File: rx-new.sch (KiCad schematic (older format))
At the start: 124 parts, among them J1 RF_IN, J2 PWR, J3 IQ_OUT, J4 4LO_IN, J5 RX_GAIN, Q1 BC848, Q2 BC858, Q3 BC848, Q4 BC858, Q5 2N7002, Q6 2N7002, U1 TPS79101DBVREP, U2 SN74CBT3253, U3 AD797, U4 AD797, U5 NC7SZ00M5X, U6 OPA1662, U7 74AUP1G74, U8 74AUP1G74, U9 4052

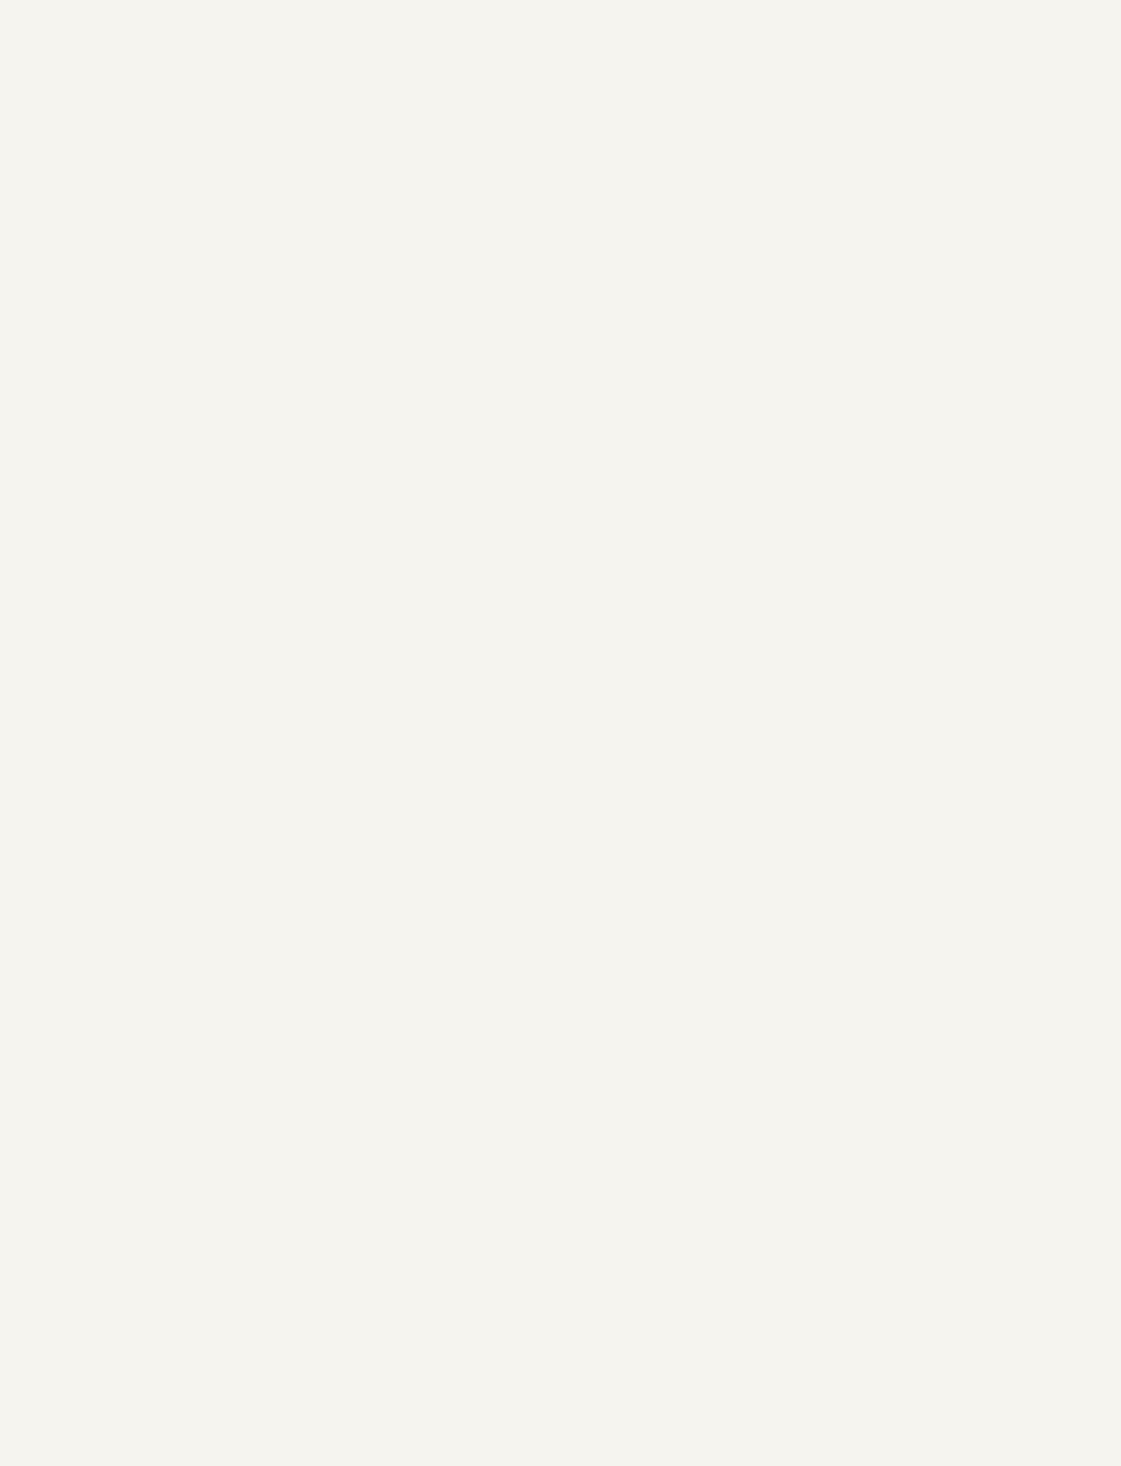
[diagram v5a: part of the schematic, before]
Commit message: WIP: added TX exciter draft
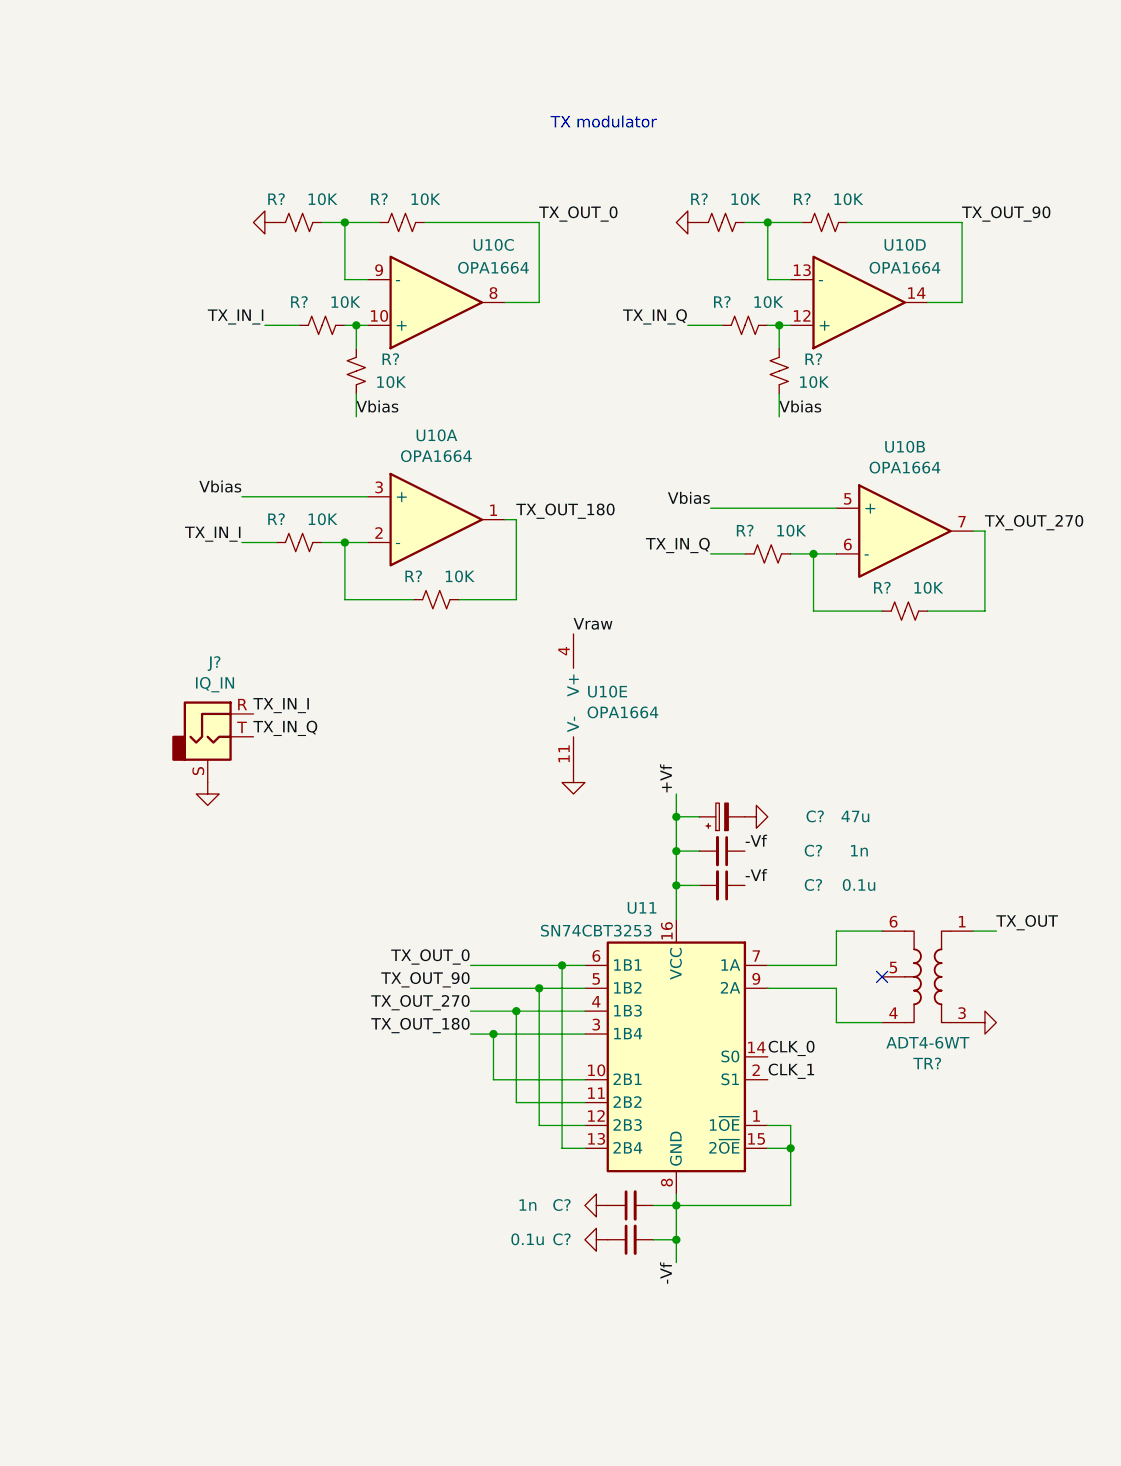
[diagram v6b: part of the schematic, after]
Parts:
- added C? (x2): 0.1u, Capacitor_SMD:C_0805_2012Metric_Pad1.15x1.40mm_HandSolder, symbol Device:C_Small
- added C? (x2): 1n, Capacitor_SMD:C_0805_2012Metric_Pad1.15x1.40mm_HandSolder, symbol Device:C_Small
- added C?: 47u, custom_library:CP_1210_3225Metric_Pad1.42x2.65mm_HandSolder, symbol Device:CP_Small
- added J?: IQ_IN, Connector_Audio:Jack_3.5mm_CUI_SJ1-3533NG_Horizontal, symbol custom_library:SJ1-3533NG
- added R? (x12): 10K, Resistor_SMD:R_0805_2012Metric_Pad1.15x1.40mm_HandSolder, symbol Device:R_Small_US
- added TR?: ADT4-6WT, RF_Mini-Circuits:Mini-Circuits_CD636_H4.11mm, symbol Transformer:ADT4-6WT
- added U10: OPA1664, symbol Device:Opamp_Quad_Generic
- added U11: SN74CBT3253, Package_SO:SOP-16_4.4x10.4mm_P1.27mm, symbol Analog_Switch:SN74CBT3253
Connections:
- net +Vf: now also C?.1, C?.2, C?.2, U11.16 (VCC)
- net -Vf: now also C?.1, C?.1, C?.2, C?.2, U11.1 (1~OE), U11.15 (2~OE), U11.8 (GND)
- net CLK_0: now also U11.14 (S0)
- net CLK_1: now also U11.2 (S1)
- net GND: now also C?.1, C?.1, C?.2, J?.S, R?.1, R?.1, TR?.3, U10.11 (V-)
- net Vbias: now also R?.2, R?.2, U10.3 (+), U10.5 (+)
- net Vraw: now also U10.4 (V+)
- new net: TR?.6, U11.7 (1A)
- new net: TR?.4, U11.9 (2A)
- new net: R?.1, R?.2, U10.2 (-)
- new net: R?.1, R?.2, U10.6 (-)
- new net: R?.1, R?.2, U10.10 (+)
- new net: R?.2, R?.2, U10.9 (-)
- new net: R?.1, R?.2, U10.12 (+)
- new net: R?.2, R?.2, U10.13 (-)
- new net TX_IN_I: J?.R, R?.1, R?.2
- new net TX_IN_Q: J?.T, R?.1, R?.2
- new net TX_OUT: TR?.1
- new net TX_OUT_0: R?.1, U10.8, U11.13 (2B4), U11.6 (1B1)
- new net TX_OUT_180: R?.1, U10.1, U11.10 (2B1), U11.3 (1B4)
- new net TX_OUT_270: R?.1, U10.7, U11.11 (2B2), U11.4 (1B3)
- new net TX_OUT_90: R?.1, U10.14, U11.12 (2B3), U11.5 (1B2)
- no-connect marks 6 -> 7
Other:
- note added: "TX modulator"

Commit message: changed_a_lot
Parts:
- removed C13: 0.01u, Capacitor_SMD:C_0805_2012Metric_Pad1.15x1.40mm_HandSolder, symbol Device:C_Small
- removed C20, C49, C?: 47u, custom_library:CP_1210_3225Metric_Pad1.42x2.65mm_HandSolder, symbol Device:CP_Small
- removed C42: 1n, Capacitor_SMD:C_0805_2012Metric_Pad1.15x1.40mm_HandSolder, symbol Device:C_Small
- removed D2: 1N4148, symbol Device:D_Small_ALT
- removed Q3: BC848, Package_TO_SOT_SMD:SOT-23, symbol Transistor_BJT:BC848
- removed R25: 100k, Resistor_SMD:R_0805_2012Metric_Pad1.15x1.40mm_HandSolder, symbol Device:R_Small_US
- removed R26, R? (x9): 10K, Resistor_SMD:R_0805_2012Metric_Pad1.15x1.40mm_HandSolder, symbol Device:R_Small_US
- removed R29: 330K, Resistor_SMD:R_0805_2012Metric_Pad1.15x1.40mm_HandSolder, symbol Device:R_Small_US
- removed R3: 1.6k, Resistor_SMD:R_0805_2012Metric_Pad1.15x1.40mm_HandSolder, symbol Device:R_Small_US
- removed R30: 180K, Resistor_SMD:R_0805_2012Metric_Pad1.15x1.40mm_HandSolder, symbol Device:R_Small_US
- removed R4: 750, Resistor_SMD:R_0805_2012Metric_Pad1.15x1.40mm_HandSolder, symbol Device:R_Small_US
- removed R8: 120k, Resistor_SMD:R_0805_2012Metric_Pad1.15x1.40mm_HandSolder, symbol Device:R_Small_US
- removed R9: 33K, Resistor_SMD:R_0805_2012Metric_Pad1.15x1.40mm_HandSolder, symbol Device:R_Small_US
- removed U1: TPS79101DBVREP, custom_library:Texas_Instruments-TPS79101DBVREP-Level_A, symbol custom_library:TPS79101DBVREP
- removed unit 2 of U10
- removed unit 3 of U10
- removed unit 4 of U10
- added C? (x6): 1n, Capacitor_SMD:C_0805_2012Metric_Pad1.15x1.40mm_HandSolder, symbol Device:C_Small
- added C? (x3): 0.1u, Capacitor_SMD:C_0805_2012Metric_Pad1.15x1.40mm_HandSolder, symbol Device:C_Small
- added C?: 47u, custom_library:CP_1210_3225Metric_Pad1.42x2.65mm_HandSolder, symbol Device:CP_Small
- added C?: NF, custom_library:CP_1210_3225Metric_Pad1.42x2.65mm_HandSolder, symbol Device:CP_Small
- added Q? (x3): BC848, Package_TO_SOT_SMD:SOT-23, symbol Transistor_BJT:BC848
- added Q?: BC327, Package_TO_SOT_THT:TO-92_Inline, symbol Transistor_BJT:BC327
- added Q? (x2): BC858, Package_TO_SOT_SMD:SOT-23, symbol Transistor_BJT:BC858
- added Q? (x4): 2N7002, Package_TO_SOT_SMD:SOT-23, symbol Transistor_FET:2N7002
- added R? (x9): 10K, Resistor_SMD:R_0805_2012Metric_Pad1.15x1.40mm_HandSolder, symbol Device:R_Small_US
- added R? (x4): 47, Resistor_SMD:R_0805_2012Metric_Pad1.15x1.40mm_HandSolder, symbol Device:R_Small_US
- added R?: 18k?, Resistor_SMD:R_0805_2012Metric_Pad1.15x1.40mm_HandSolder, symbol Device:R_Small_US
- added R? (x2): 10k, Resistor_SMD:R_0805_2012Metric_Pad1.15x1.40mm_HandSolder, symbol Device:R_Small_US
- added R?: 27k, Resistor_SMD:R_0805_2012Metric_Pad1.15x1.40mm_HandSolder, symbol Device:R_Small_US
- added R?: 1.8k, Resistor_SMD:R_0805_2012Metric_Pad1.15x1.40mm_HandSolder, symbol Device:R_Small_US
- added R? (x5): 1M, Resistor_SMD:R_0805_2012Metric_Pad1.15x1.40mm_HandSolder, symbol Device:R_Small_US
- added R?: 100k, Resistor_SMD:R_0805_2012Metric_Pad1.15x1.40mm_HandSolder, symbol Device:R_Small_US
- added R? (x3): 330k, Resistor_SMD:R_0805_2012Metric_Pad1.15x1.40mm_HandSolder, symbol Device:R_Small_US
- added R?: 1E, Resistor_SMD:R_0805_2012Metric_Pad1.15x1.40mm_HandSolder, symbol Device:R_Small_US
- added R? (x2): 820k, Resistor_SMD:R_0805_2012Metric_Pad1.15x1.40mm_HandSolder, symbol Device:R_Small_US
- added R?: 47k, Resistor_SMD:R_0805_2012Metric_Pad1.15x1.40mm_HandSolder, symbol Device:R_Small_US
- added R? (x3): NF, Resistor_SMD:R_0805_2012Metric_Pad1.15x1.40mm_HandSolder, symbol Device:R_Small_US
- added R?: 27E, Resistor_SMD:R_0805_2012Metric_Pad1.15x1.40mm_HandSolder, symbol Device:R_Small_US
- added R? (x2): 33k, Resistor_SMD:R_0805_2012Metric_Pad1.15x1.40mm_HandSolder, symbol Device:R_Small_US
- added U? (x3): OPA1664, symbol Device:Opamp_Quad_Generic
- added U?: LM4040DBZ-3, Package_TO_SOT_SMD:SOT-23, symbol Reference_Voltage:LM4040DBZ-3
- C30: value 47u -> NF
- R10: value 10k -> 33k
- R11: value 10k -> 33kk
- R27: value 10k -> 100k
- R28: value 47k -> 330k
- R6: value 10k -> NF
- R7: value 22E -> 1E
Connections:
- net +9V: no longer C50.2, C51.2, R12.2, R13.2, U9.16 (VDD)
- net +Vd: now also R5.2; no longer R5.1
- net +Vf: now also C50.2, C51.2, R12.2, R13.2, R?.2, U9.16 (VDD), C?.2, Q?.1 (C), Q?.2 (E), R?.1, R?.1, R?.1, R?.1, R?.2, R?.2, R?.2, R?.2
- net -Vf: now also R?.2; no longer U11.1 (1~OE), U11.15 (2~OE), U2.1 (1~OE), U2.15 (2~OE)
- net 270deg: no longer R39.2, R40.2, R41.2, R42.2
- net 90deg: now also R39.2, R40.2, R41.2, R42.2
- net Eo: now also Q?.3 (D), Q?.3 (D), R?.1
- net GND: now also C?.1, C?.1, C?.1, C?.1, C?.1, C?.1, C?.1, C?.1, C?.2, C?.2, Q?.2 (E), Q?.2 (S), Q?.2 (S), Q?.2 (S), Q?.2 (S), R?.1, R?.1, R?.1, R?.1, R?.1, R?.2, R?.2, R?.2, R?.2, U?.2 (A)
- net Vbat: now also Q4.2 (E), R27.2, Q?.2 (E), Q?.3 (C), Q?.3 (E), R?.1
- net at C30.1, C31.2, C32.2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: no longer C34.2, C35.2, U4.7 (V+)
- net at C4.1, Q2.1 (B): now also R?.2
- net at C1.1, Q1.2 (E): now also R5.1; no longer R5.2
- net at R13.1, U9.9 (B): now also R34.1; no longer R34.2
- net at Q6.3 (D): now also R34.2; no longer R34.1
- net at R?.1, R?.2, U10.2 (-): now also R?.1, R?.1
- net En renamed EnTx
- net EnTx: now also R?.2
- net FB_SEL_1 renamed Gain_0
- net Gain_0: now also R?.2
- net FB_SEL_2 renamed Gain_1
- net Gain_1: now also R?.2
- net OPAMP1_OUT renamed OP1_O
- net OPAMP2_OUT renamed OP2_O
- net TX_IN_I renamed TX_I
- net TX_IN_Q renamed TX_Q
- net TX_Q: now also R?.2
- net TX_OUT_0: no longer names the net of U11.13 (2B4), U11.6 (1B1)
- net TX_OUT_0: now also C?.2, R?.1
- net TX_OUT_180: no longer names the net of U11.10 (2B1), U11.3 (1B4)
- net TX_OUT_180: now also C?.2, R?.1; no longer R?.1, U10.1
- net TX_OUT_270: no longer names the net of U11.11 (2B2), U11.4 (1B3)
- net TX_OUT_270: now also C?.2, R?.1
- net TX_OUT_90: no longer names the net of U11.12 (2B3), U11.5 (1B2)
- net TX_OUT_90: now also C?.2, R?.1
- net Vbias renamed Rxbias
- net Rxbias: now also R?.1; no longer C52.2, C53.2, R?.2, U10.3 (+), U9.6 (Inh), U9.8 (VSS)
- removed net Vraw: J2.4 (Pin_4), Q4.2 (E), R27.2, U10.4 (V+)
- new net: R?.1, R?.2, U2.1 (1~OE), U2.15 (2~OE)
- new net: R?.1, R?.2, U?.6 (-)
- new net: R?.1, R?.1, R?.1, R?.2, U?.9 (-)
- new net: R?.1, R?.2, U?.13 (-)
- new net: C?.1, Q?.1 (B), R?.1, R?.2
- new net: Q?.2 (E), Q?.2 (E), R?.1
- new net: Q?.2 (B), Q?.3 (C)
- new net: R?.1, R?.2, U11.1 (1~OE), U11.15 (2~OE)
- new net: Q?.3 (C), R?.1
- new net: Q?.1 (B), R?.2, R?.2, R?.2
- new net: Q?.1 (B), R?.1, R?.2 (x2)
- new net: Q?.3 (C), R?.2
- new net: Q?.3 (D), R?.2 (x2)
- new net: C?.1, C?.2, C?.2, Q?.3 (C)
- new net EnRX: Q?.1 (G), Q?.1 (G), R?.1
- new net EnRx: J2.4 (Pin_4), R?.2
- new net EnTX: Q?.1 (G), Q?.1 (G), R?.1
- new net RXbias: C52.2, C53.2, U9.6 (Inh), U9.8 (VSS)
- new net TX_0: R?.1, R?.2, U?.7
- new net TX_180: R?.1, R?.2, R?.2, U10.1
- new net TX_270: R?.1, R?.1, R?.2, R?.2, U?.14, U?.8
- new net TX_90: R?.2
- new net Txbias: C?.2, C?.2, R?.1, R?.1, R?.2, U10.3 (+), U?.10 (+), U?.12 (+), U?.5 (+)
- new net VopRX: C34.2, C35.2, U4.7 (V+)
- new net VopTX: U10.4 (V+)
- new net Vref: C?.1, Q?.1 (B), R?.1, R?.2, U?.1 (K)
- no-connect marks 7 -> 8
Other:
- note added: "3.7V"
- note added: "6.9V"
- note added: "8.7V"
- note added: "Binary 00 = highest gain, 11 = lowest gain.\nSwap 4 R's to invert this choice."
- note removed: "+Vd = 6.9V"
- note removed: "+Vf = 8.53V"
- note removed: "-Vf = 3.47V"
- note removed: "Every supply C should be a tripple, high value (47µF, mid 0.1µf, small 1nF)"
- moved on the sheet: C1, C10, C11, C12, C14, C15, C16, C17, C18, C19, C2, C21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

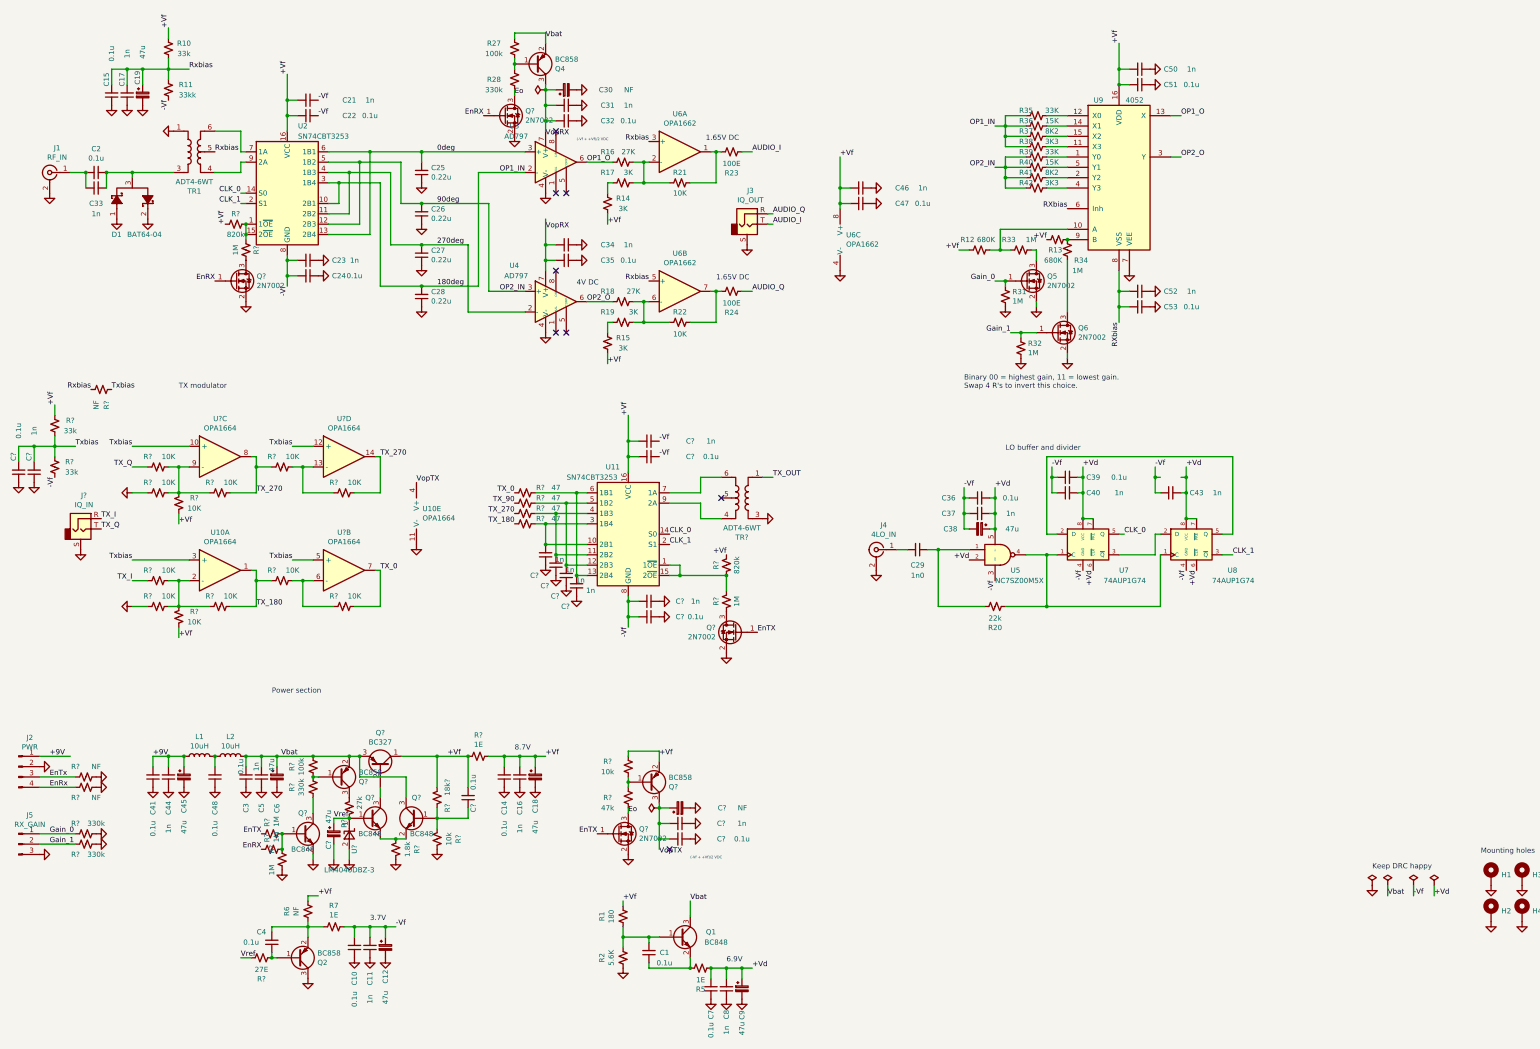
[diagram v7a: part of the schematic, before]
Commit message: Annotations, cleaning up, made ERC pass
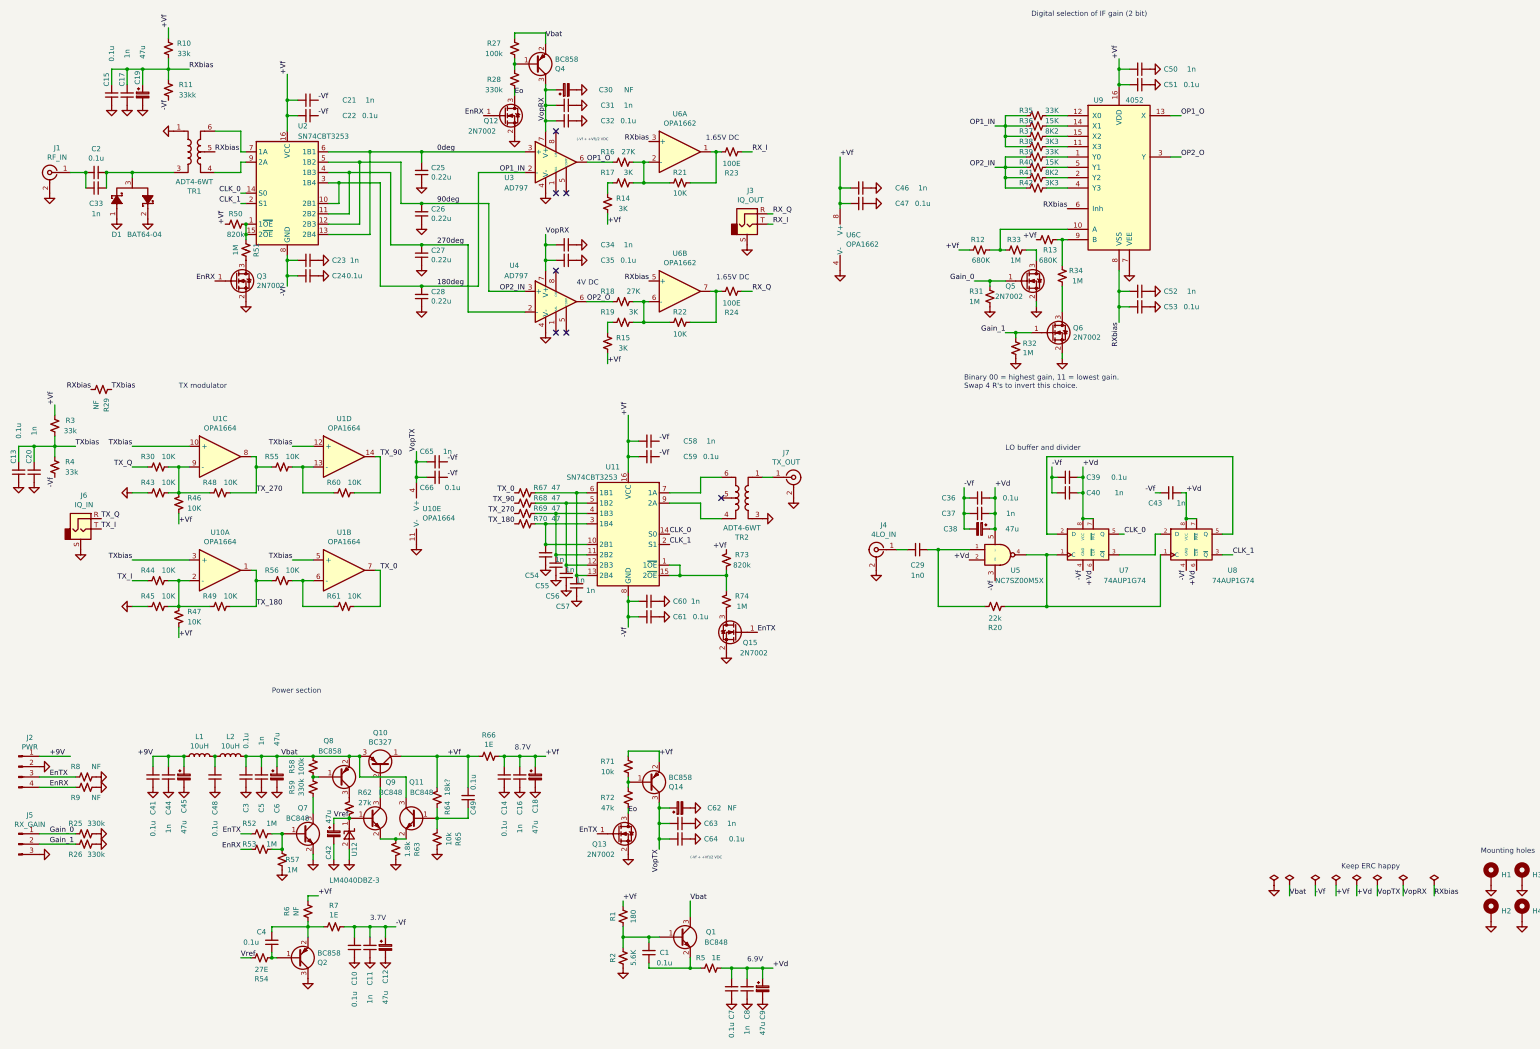
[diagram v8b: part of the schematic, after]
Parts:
- added C65: 1n, Capacitor_SMD:C_0805_2012Metric_Pad1.15x1.40mm_HandSolder, symbol Device:C_Small
- added C66: 0.1u, Capacitor_SMD:C_0805_2012Metric_Pad1.15x1.40mm_HandSolder, symbol Device:C_Small
- added J7: TX_OUT, Connector_Coaxial:SMA_Amphenol_901-144_Vertical, symbol Connector:Conn_Coaxial
- gave numbers to parts that had none: 69
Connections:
- net EnRx is gone; now on net EnRX: J2.4 (Pin_4), R9.2
- net EnTx is gone; now on net EnTX: J2.3 (Pin_3), R8.2
- net Rxbias is gone; now on net RXbias: C15.2, C17.2, C19.1, R10.1, R11.1, R29.1, TR1.5, U6.3 (+), U6.5 (+)
- net -Vf: now also C65.1, C66.1
- net GND: now also J7.2 (Ext)
- net TX_270: no longer R60.1, U1.14
- net TX_90: now also R60.1, U1.14
- net TX_I: now also J6.T; no longer J6.R
- net TX_Q: now also J6.R; no longer J6.T
- net VopRX: now also C30.1, C31.2, C32.2, Q4.3 (C), U3.7 (V+)
- net VopTX: now also C62.1, C63.2, C64.2, Q14.3 (C), C65.2, C66.2
- net AUDIO_I renamed RX_I
- net AUDIO_Q renamed RX_Q
- net TX_OUT: no longer names the net of TR2.1
- net TX_OUT: now also J7.1 (In)
- net Txbias renamed TXbias
- no-connect marks 8 -> 7
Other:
- note added: "Digital selection of IF gain (2 bit)"
- note added: "Keep ERC happy"
- note removed: "Keep DRC happy"
- moved on the sheet: C7, C8, C9, Q6, R13, R31, R32, R33, R34, R5, R52, R53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
